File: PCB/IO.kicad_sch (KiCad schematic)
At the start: 14 parts, among them J601 USB_C_Receptacle_USB2.0_16P, J602 Conn_02x03_Counter_Clockwise, J603 Screw_Terminal_01x08, J604 Conn_01x02_Pin, J605 Conn_01x05, J606 Conn_02x03_Counter_Clockwise, J607 Conn_01x04

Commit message: Created Bill of materials for the computer
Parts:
- G601, J605: now left out of the parts list
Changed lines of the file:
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@@
 		(unit 1)
 		(exclude_from_sim no)
-		(in_bom yes)
+		(in_bom no)
 		(on_board yes)
 		(dnp no)
@@
 		(unit 1)
 		(exclude_from_sim no)
-		(in_bom yes)
-		(on_board yes)
-		(dnp no)
+		(in_bom no)
+		(on_board yes)
+		(dnp no)

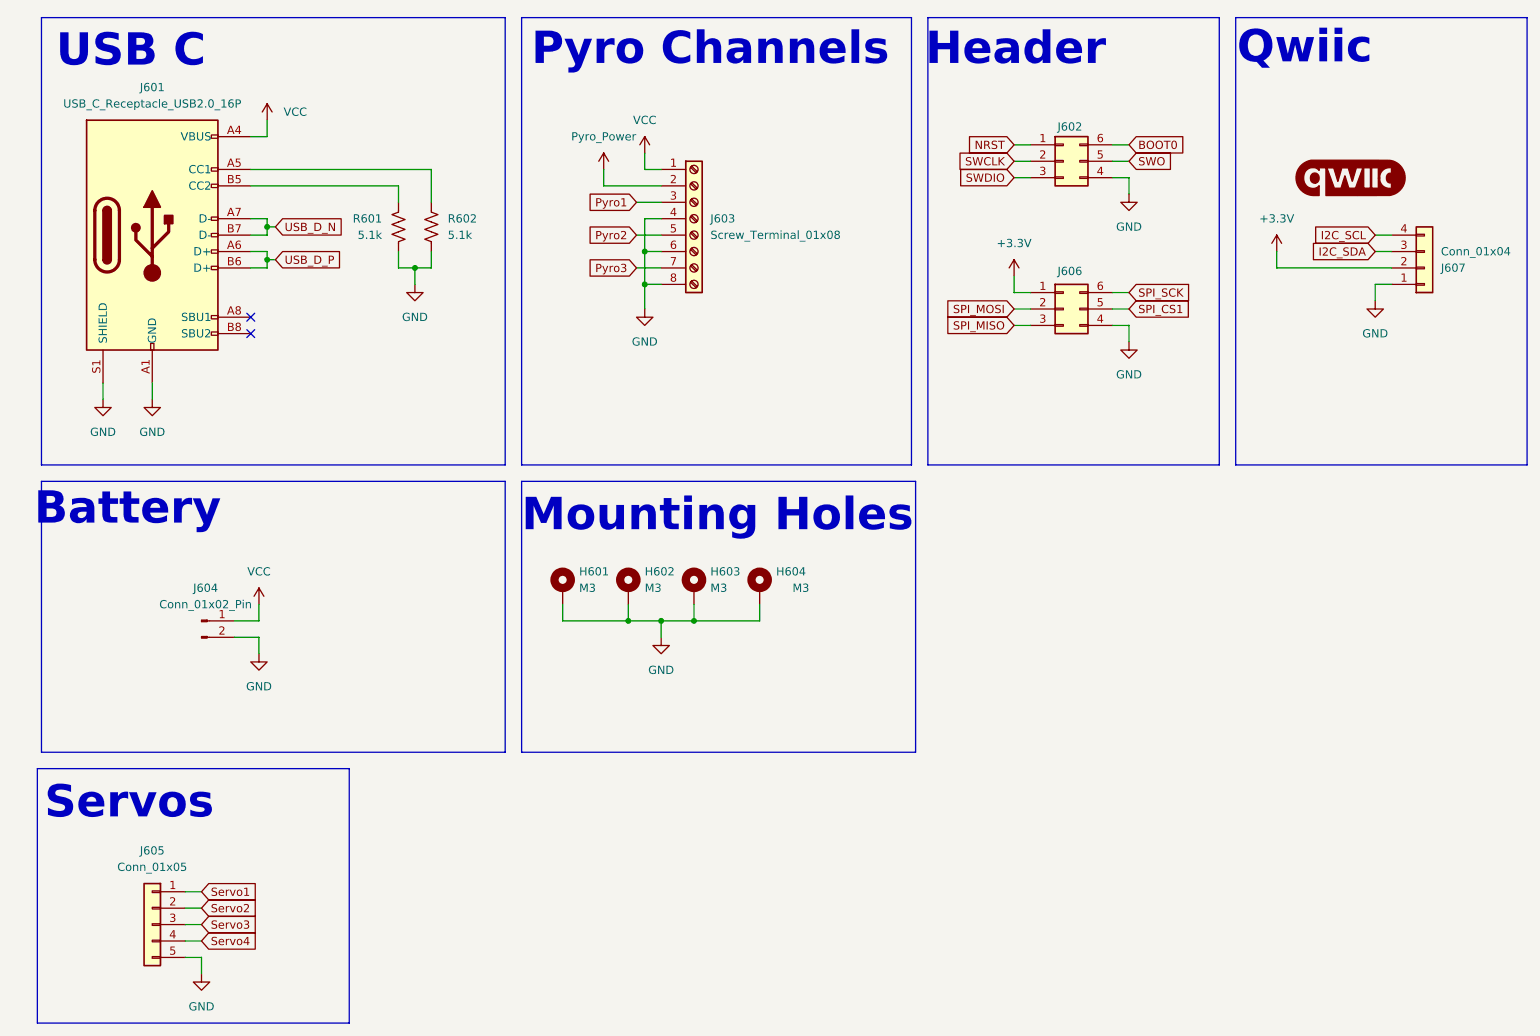
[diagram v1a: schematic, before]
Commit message: Cleaned up the schematic and replace and rerouted everything, also replace radio with a module
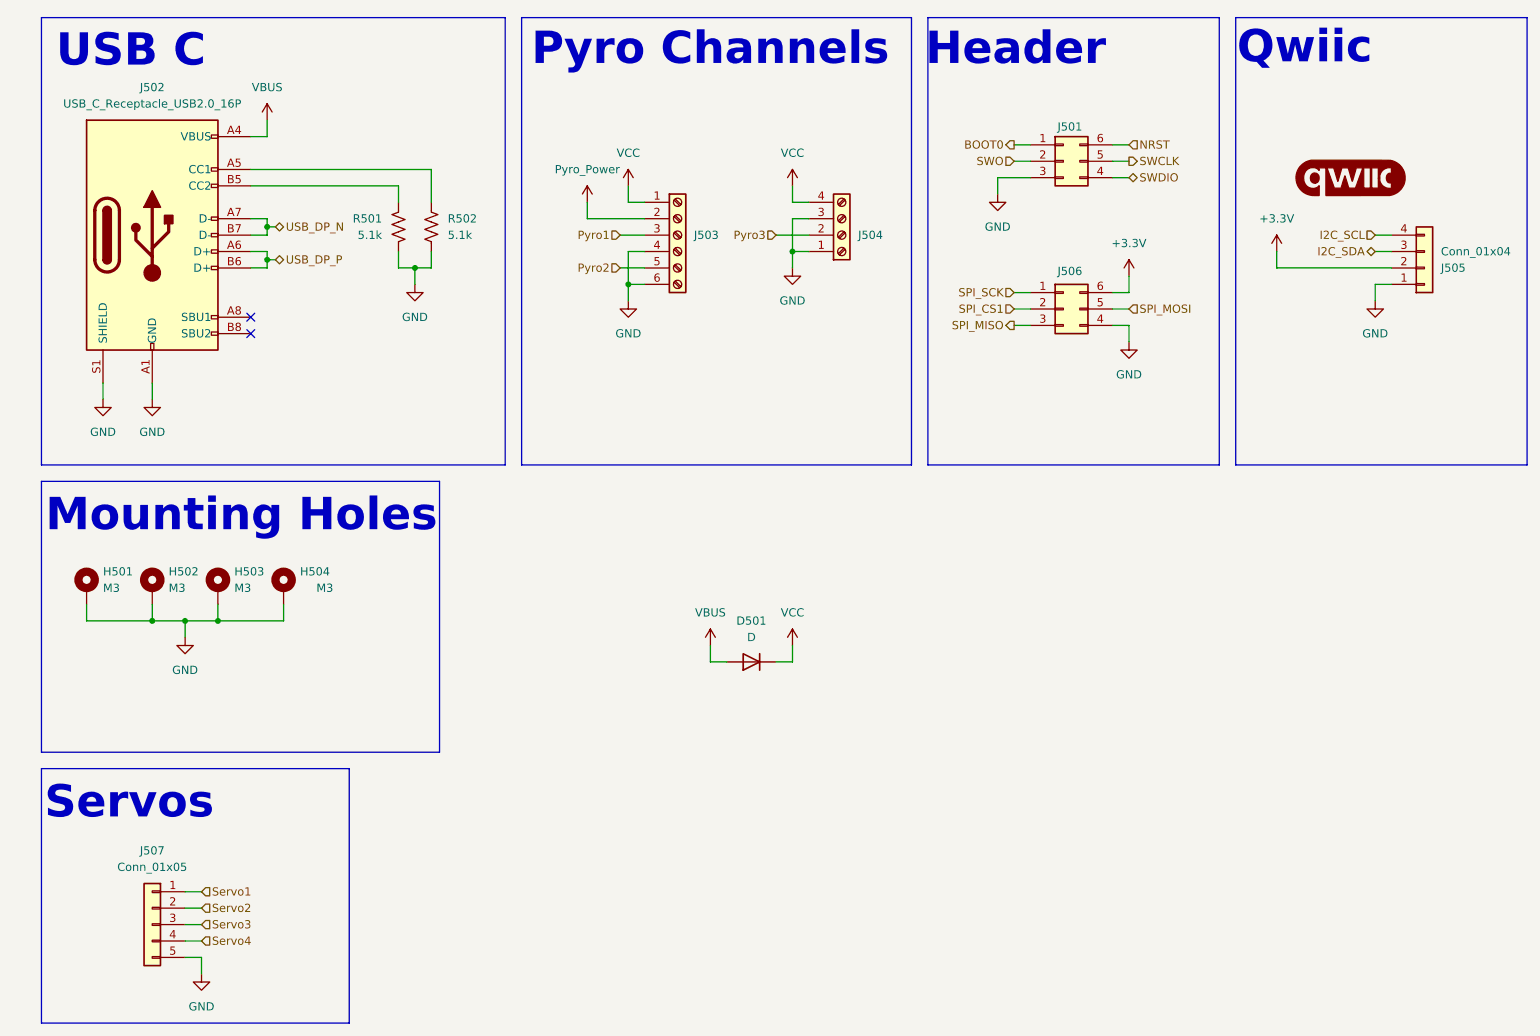
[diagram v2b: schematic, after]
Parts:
- removed J603: Screw_Terminal_01x08, TerminalBlock_Phoenix:TerminalBlock_Phoenix_MPT-0,5-8-2.54_1x08_P2.54mm_Horizontal, symbol Connector:Screw_Terminal_01x08
- removed J604: Conn_01x02_Pin, Connector_PinHeader_2.54mm:PinHeader_1x02_P2.54mm_Vertical, symbol Connector:Conn_01x02_Pin
- added D501: D, Package_TO_SOT_SMD:SOT-23, symbol Device:D
- added J503: Screw_Terminal_01x06, TerminalBlock_Phoenix:TerminalBlock_Phoenix_MPT-0,5-6-2.54_1x06_P2.54mm_Horizontal, symbol Connector:Screw_Terminal_01x06
- added J504: Screw_Terminal_01x04, TerminalBlock_Phoenix:TerminalBlock_Phoenix_MPT-0,5-4-2.54_1x04_P2.54mm_Horizontal, symbol Connector:Screw_Terminal_01x04
- renumbered G601 to G501, H601 to H501, H602 to H502, H603 to H503, H604 to H504, J602 to J501, J601 to J502, J607 to J505, J606 to J506, J605 to J507, R601 to R501, R602 to R502
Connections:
- net +3.3V: now also J506.6 (Pin_6); no longer J506.1 (Pin_1)
- net BOOT0: now also J501.1 (Pin_1); no longer J501.6 (Pin_6)
- net GND: now also J501.3 (Pin_3), J503.4 (Pin_4), J503.6 (Pin_6), J504.1 (Pin_1), J504.3 (Pin_3); no longer J501.4 (Pin_4)
- net NRST: now also J501.6 (Pin_6); no longer J501.1 (Pin_1)
- net Pyro1: now also J503.3 (Pin_3)
- net Pyro2: now also J503.5 (Pin_5)
- net Pyro3: now also J504.2 (Pin_2)
- net Pyro_Power: now also J503.2 (Pin_2)
- net SPI_CS1: now also J506.2 (Pin_2); no longer J506.5 (Pin_5)
- net SPI_MOSI: now also J506.5 (Pin_5); no longer J506.2 (Pin_2)
- net SPI_SCK: now also J506.1 (Pin_1); no longer J506.6 (Pin_6)
- net SWCLK: now also J501.5 (Pin_5); no longer J501.2 (Pin_2)
- net SWDIO: now also J501.4 (Pin_4); no longer J501.3 (Pin_3)
- net SWO: now also J501.2 (Pin_2); no longer J501.5 (Pin_5)
- net VCC: now also D501.3 (K), J503.1 (Pin_1), J504.4 (Pin_4); no longer J502.A4 (VBUS), J502.A9 (VBUS), J502.B4 (VBUS), J502.B9 (VBUS)
- net USB_D_N renamed USB_DP_N
- net USB_D_P renamed USB_DP_P
- new net VBUS: D501.1 (A), J502.A4 (VBUS), J502.A9 (VBUS), J502.B4 (VBUS), J502.B9 (VBUS)
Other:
- note removed: "Battery"
- moved on the sheet: H501, H502, H503, H504

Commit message: Updated BOM Added logo to PCB Reexported schematic
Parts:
- J501, J506: now left out of the parts list
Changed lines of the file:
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@@
 		(unit 1)
 		(exclude_from_sim no)
-		(in_bom yes)
+		(in_bom no)
 		(on_board yes)
 		(dnp no)
@@
 		(unit 1)
 		(exclude_from_sim no)
-		(in_bom yes)
-		(on_board yes)
-		(dnp no)
+		(in_bom no)
+		(on_board yes)
+		(dnp no)

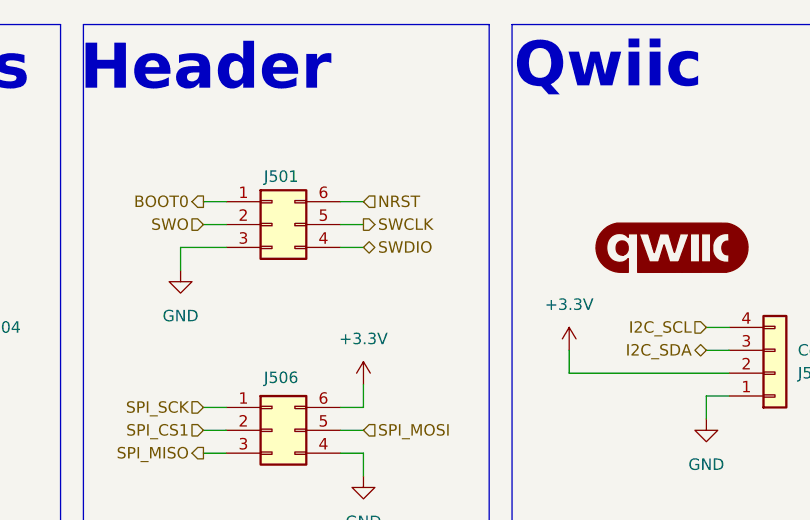
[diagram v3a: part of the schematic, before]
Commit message: Fixed SWD pinout Updated CubeMX Project
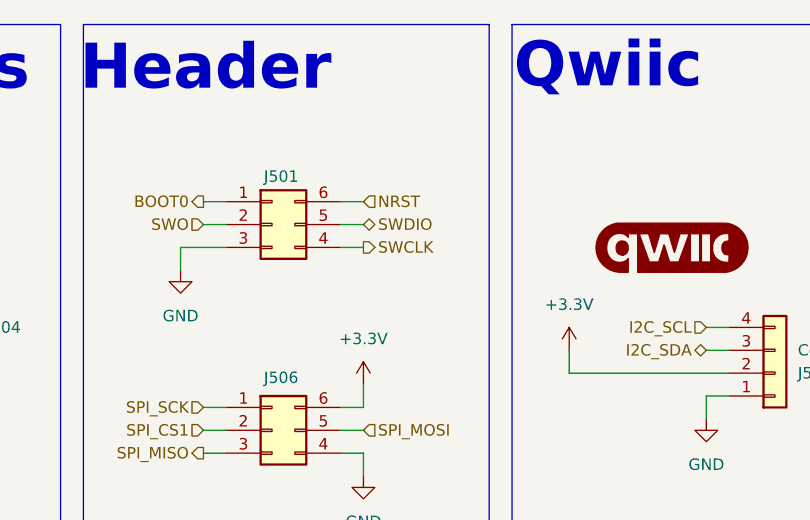
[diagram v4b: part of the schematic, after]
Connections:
- net SWCLK: now also J501.4 (Pin_4); no longer J501.5 (Pin_5)
- net SWDIO: now also J501.5 (Pin_5); no longer J501.4 (Pin_4)
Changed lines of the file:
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@@
 	(hierarchical_label "SWDIO"
 		(shape bidirectional)
-		(at 182.88 39.37 0)
+		(at 182.88 36.83 0)
 		(effects
 			(font
@@
 	(hierarchical_label "SWCLK"
 		(shape output)
-		(at 182.88 36.83 0)
+		(at 182.88 39.37 0)
 		(effects
 			(font

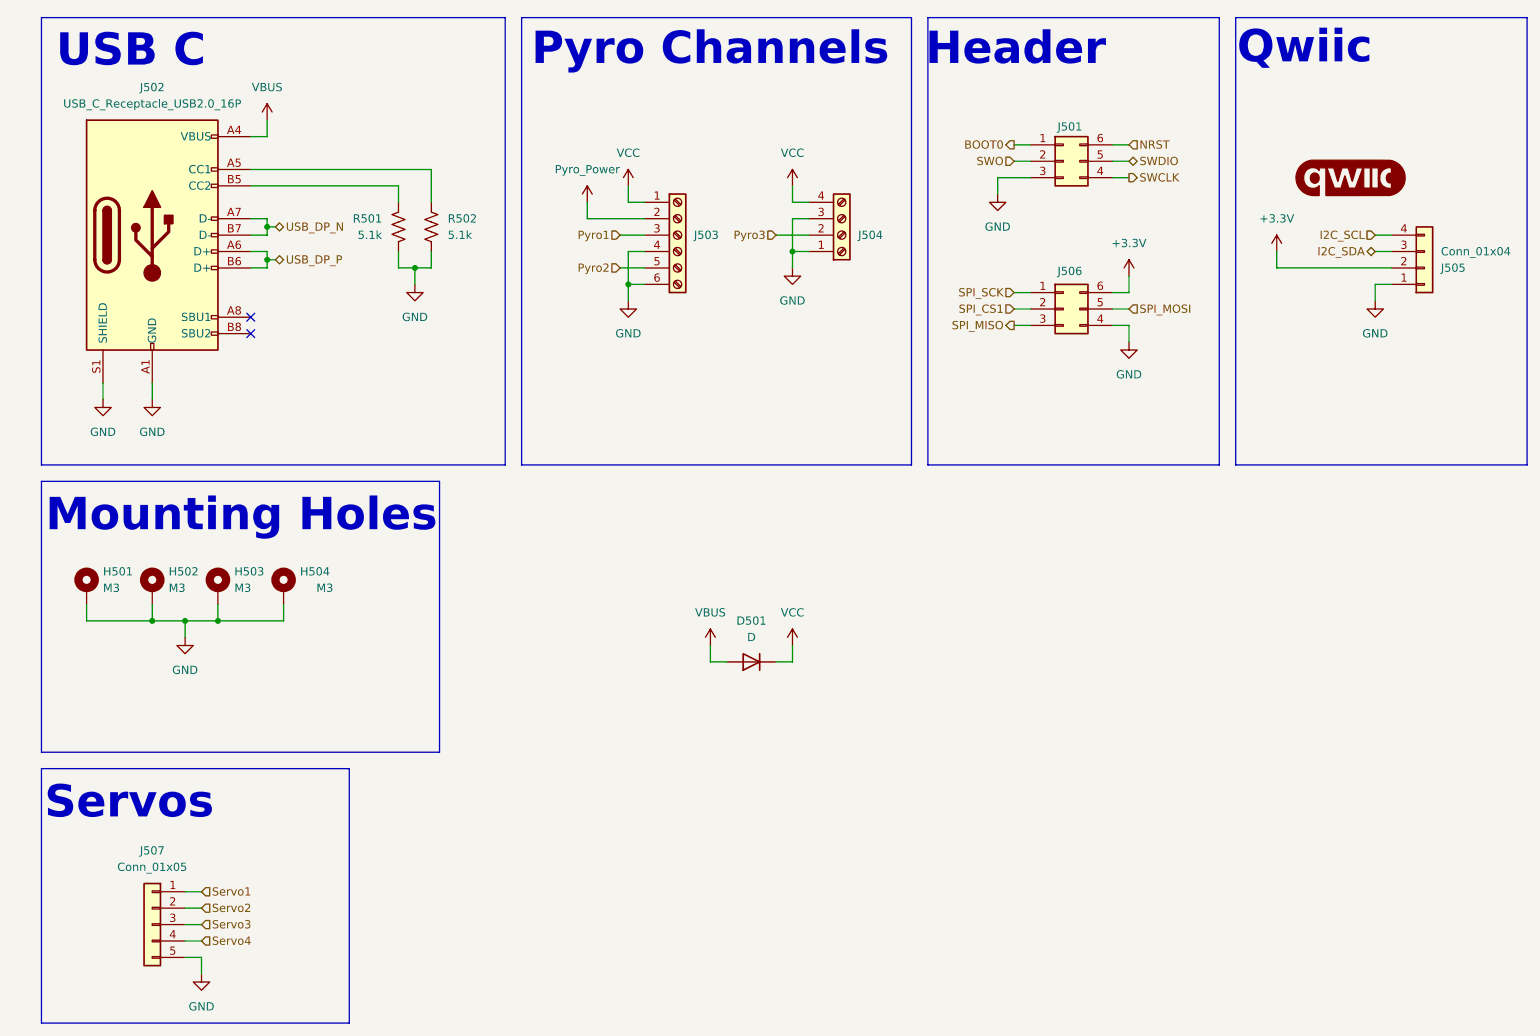
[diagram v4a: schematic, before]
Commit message: Switch from high side switch to low side switch for pyro channels
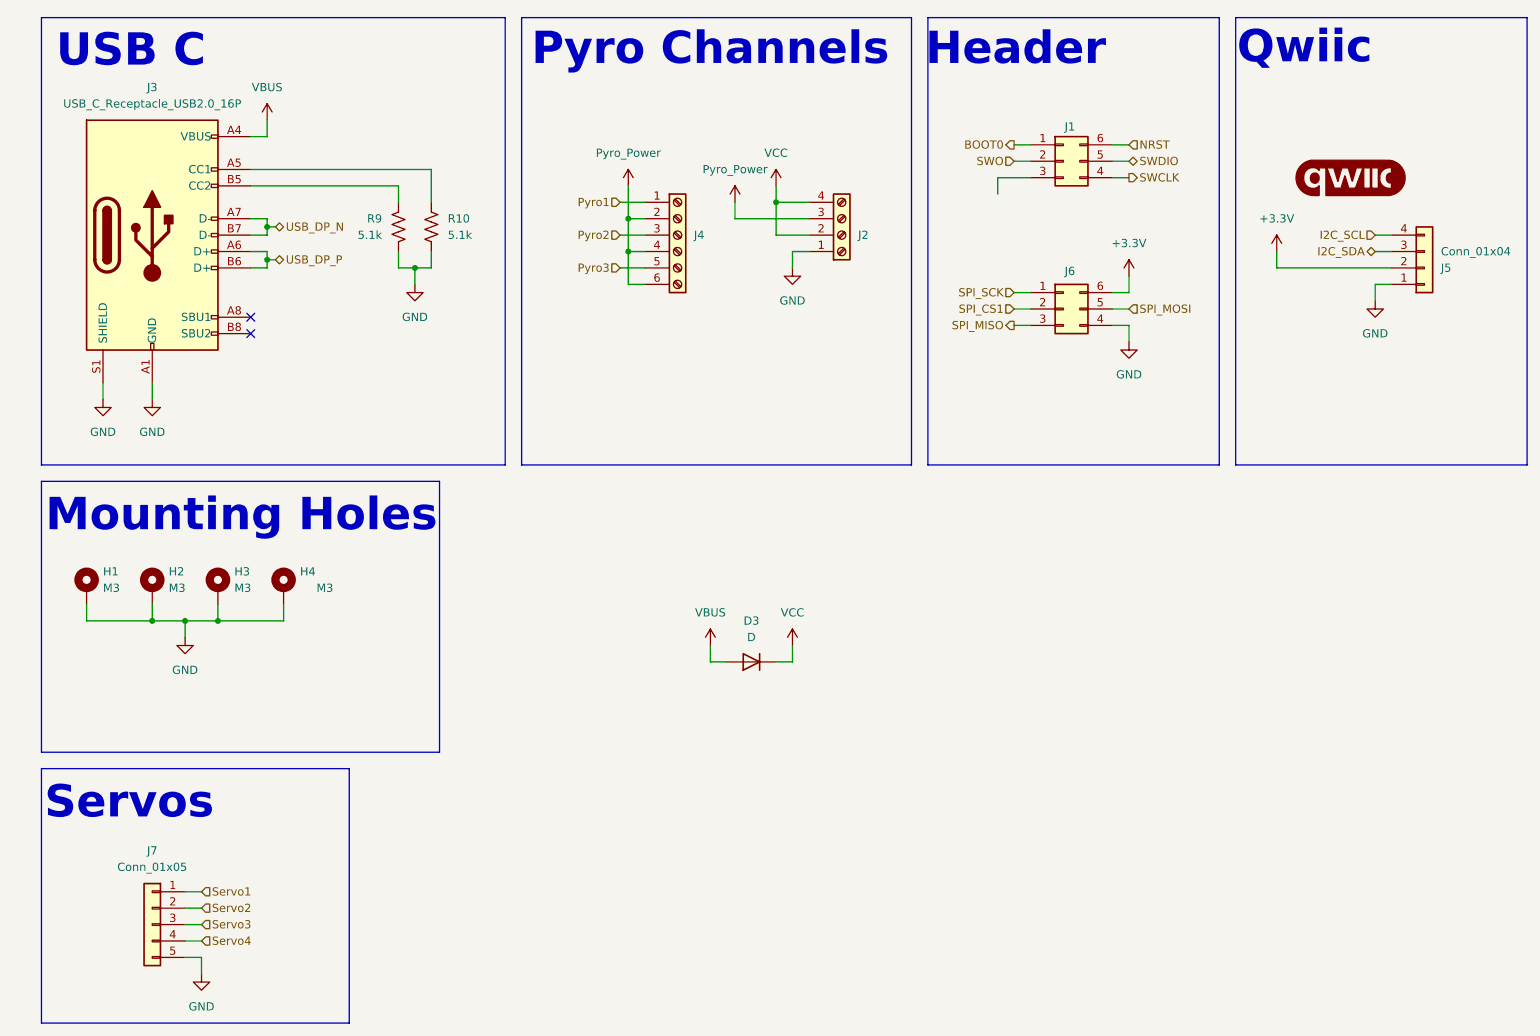
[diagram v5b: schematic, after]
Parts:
- renumbered D501 to D3, G501 to G1, H501 to H1, H502 to H2, H503 to H3, H504 to H4, J501 to J1, J504 to J2, J502 to J3, J503 to J4, J505 to J5, J506 to J6, J507 to J7, R502 to R10, R501 to R9
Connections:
- net GND: no longer J1.3 (Pin_3), J2.3 (Pin_3), J4.4 (Pin_4), J4.6 (Pin_6)
- net Pyro1: now also J4.1 (Pin_1); no longer J4.3 (Pin_3)
- net Pyro2: now also J4.3 (Pin_3); no longer J4.5 (Pin_5)
- net Pyro3: now also J4.5 (Pin_5); no longer J2.2 (Pin_2)
- net Pyro_Power: now also J2.3 (Pin_3), J4.4 (Pin_4), J4.6 (Pin_6)
- net VCC: now also J2.2 (Pin_2); no longer J4.1 (Pin_1)

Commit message: Fixed component annotation Updated BOM to reflect the pyro channel changes Updates Production files
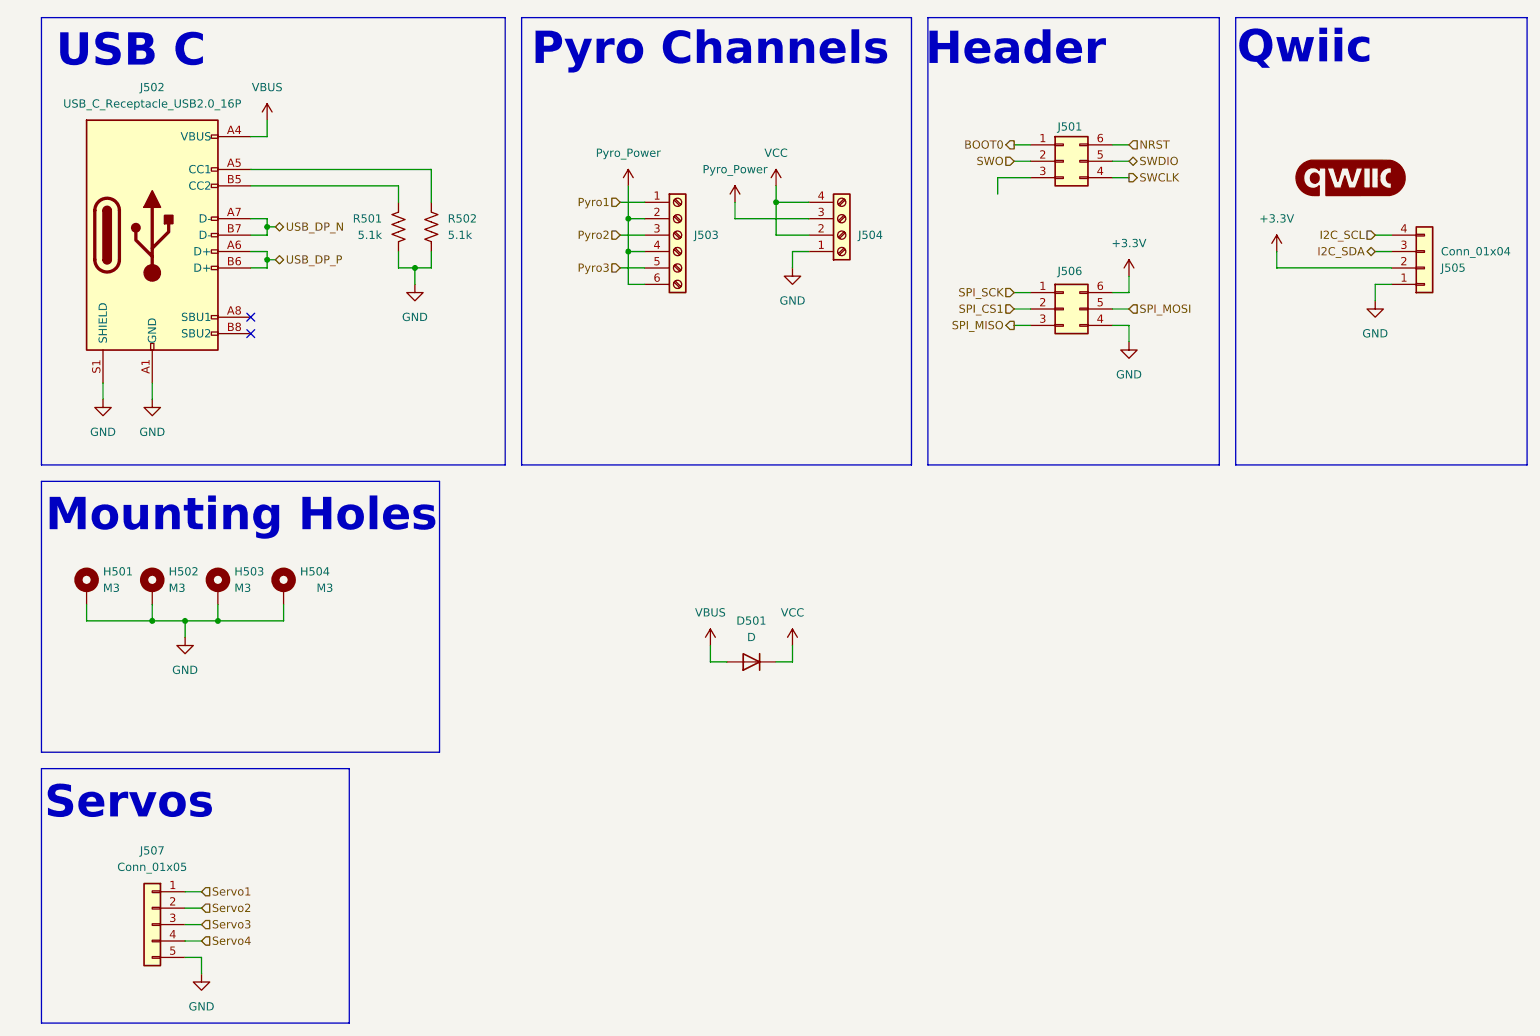
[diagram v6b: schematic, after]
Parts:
- renumbered D3 to D501, G1 to G501, H1 to H501, H2 to H502, H3 to H503, H4 to H504, J1 to J501, J3 to J502, J4 to J503, J2 to J504, J5 to J505, J6 to J506, J7 to J507, R9 to R501, R10 to R502
